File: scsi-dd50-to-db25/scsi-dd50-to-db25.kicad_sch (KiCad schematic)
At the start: 2 parts, among them J1 DD50_Plug_MountingHoles, J2 DB25_Socket_MountingHoles

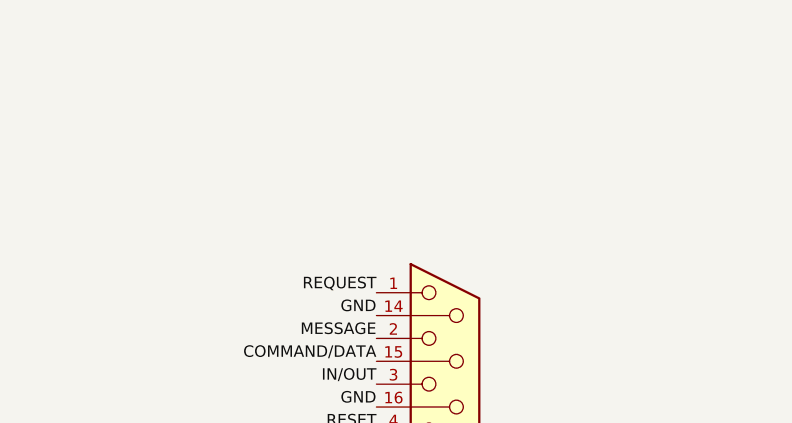
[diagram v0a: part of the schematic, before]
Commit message: Added a term power port for pulling 5v off to another adapter.
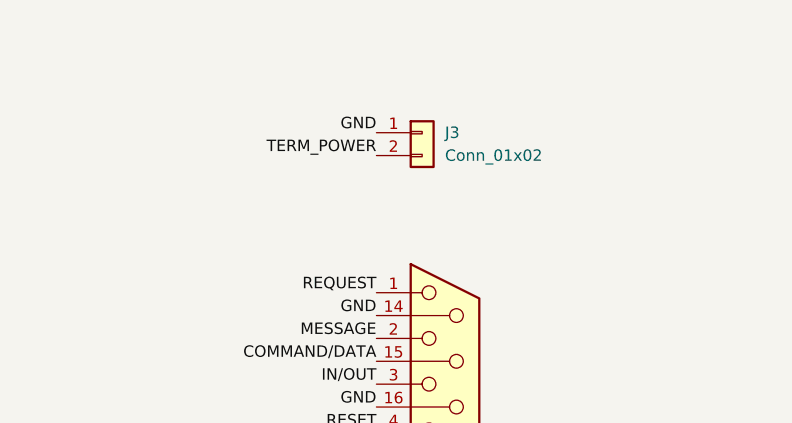
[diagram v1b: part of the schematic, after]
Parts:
- added J3: Conn_01x02, Connector_PinHeader_2.54mm:PinHeader_1x02_P2.54mm_Horizontal, symbol Connector_Generic:Conn_01x02
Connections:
- net GND: now also J3.1 (Pin_1)
- net TERM_POWER: now also J3.2 (Pin_2)
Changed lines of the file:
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@@
+		)
+	)
+	(label "GND"
+		(at 167.64 45.72 180)
+		(effects
+			(font
+				(size 1.27 1.27)
+			)
+			(justify right bottom)
 		)
 	)
 	(label "TERM_POWER"
 		(at 167.64 121.92 180)
+		(effects
+			(font
+				(size 1.27 1.27)
+			)
+			(justify right bottom)
+		)
+	)
+	(label "TERM_POWER"
+		(at 167.64 48.26 180)
 		(effects
 			(font
@@
 					(unit 1)
 				)
+			)
+		)
+	)
+	(symbol
+		(lib_id "Connector_Generic:Conn_01x02")
+		(at 172.72 45.72 0)
+		(unit 1)
+		(exclude_from_sim no)
+		(in_bom yes)
+		(on_board yes)
+		(dnp no)
+		(fields_autoplaced yes)
+		(property "Reference" "J3"
+			(at 175.26 45.7199 0)
+			(effects
+				(font
+					(size 1.27 1.27)
+				)
+				(justify left)
+			)
+		)
+		(property "Value" "Conn_01x02"
+			(at 175.26 48.2599 0)
+			(effects
+				(font
+					(size 1.27 1.27)
+				)
+				(justify left)
+			)
+		)
+		(property "Footprint" "Connector_PinHeader_2.54mm:PinHeader_1x02_P2.54mm_Horizontal"
+			(at 172.72 45.72 0)
+			(effects
+				(font
+					(size 1.27 1.27)
+				)
+				(hide yes)
+			)
+		)
+		(property "Datasheet" "~"
+			(at 172.72 45.72 0)
+			(effects
+				(font
+					(size 1.27 1.27)
+				)
+				(hide yes)
+			)
+		)
+		(property "Description" "Generic connector, single row, 01x02, script generated (kicad-library-utils/schlib/autogen/connector/)"
+			(at 172.72 45.72 0)
+			(effects
+				(font
+					(size 1.27 1.27)
+				)
+				(hide yes)
+			)
+		)
+		(pin "1"
+		)
+		(pin "2"
+		)
+		(instances
+			(project ""
+				(path "/4355ec7a-8fe5-41c6-bf79-94b58d7f3796"
+					(reference "J3")
+					(unit 1)
+				)

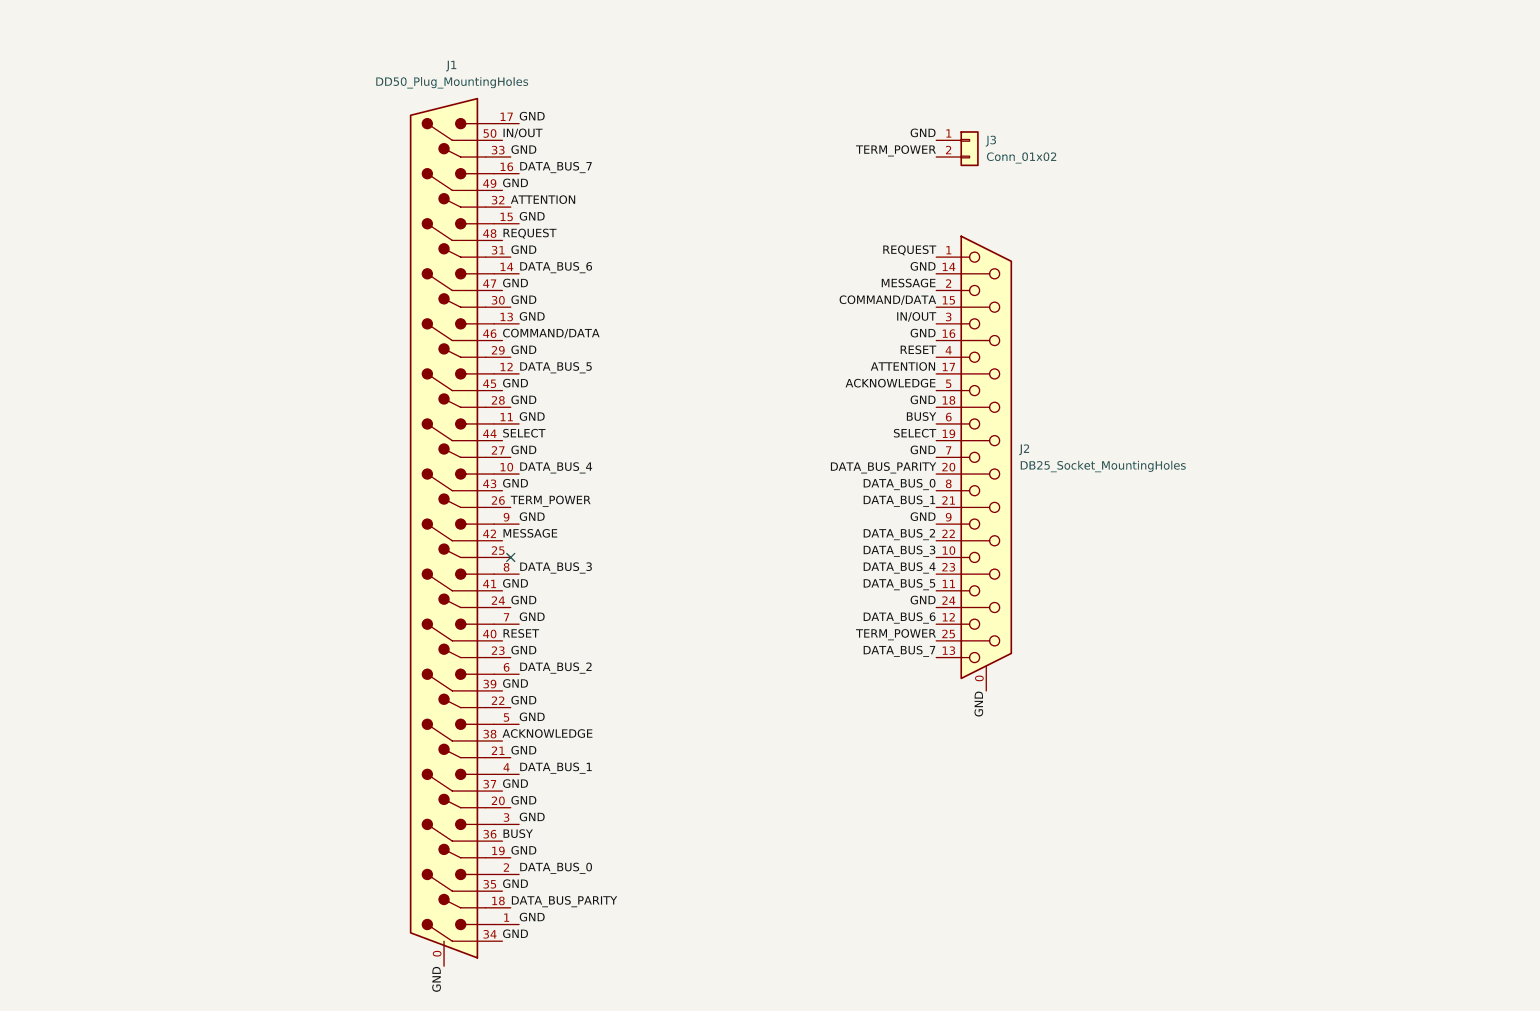
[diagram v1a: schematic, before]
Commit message: Fixing the pinout of the Sun Microsystems SCSI SE DD50 connector.
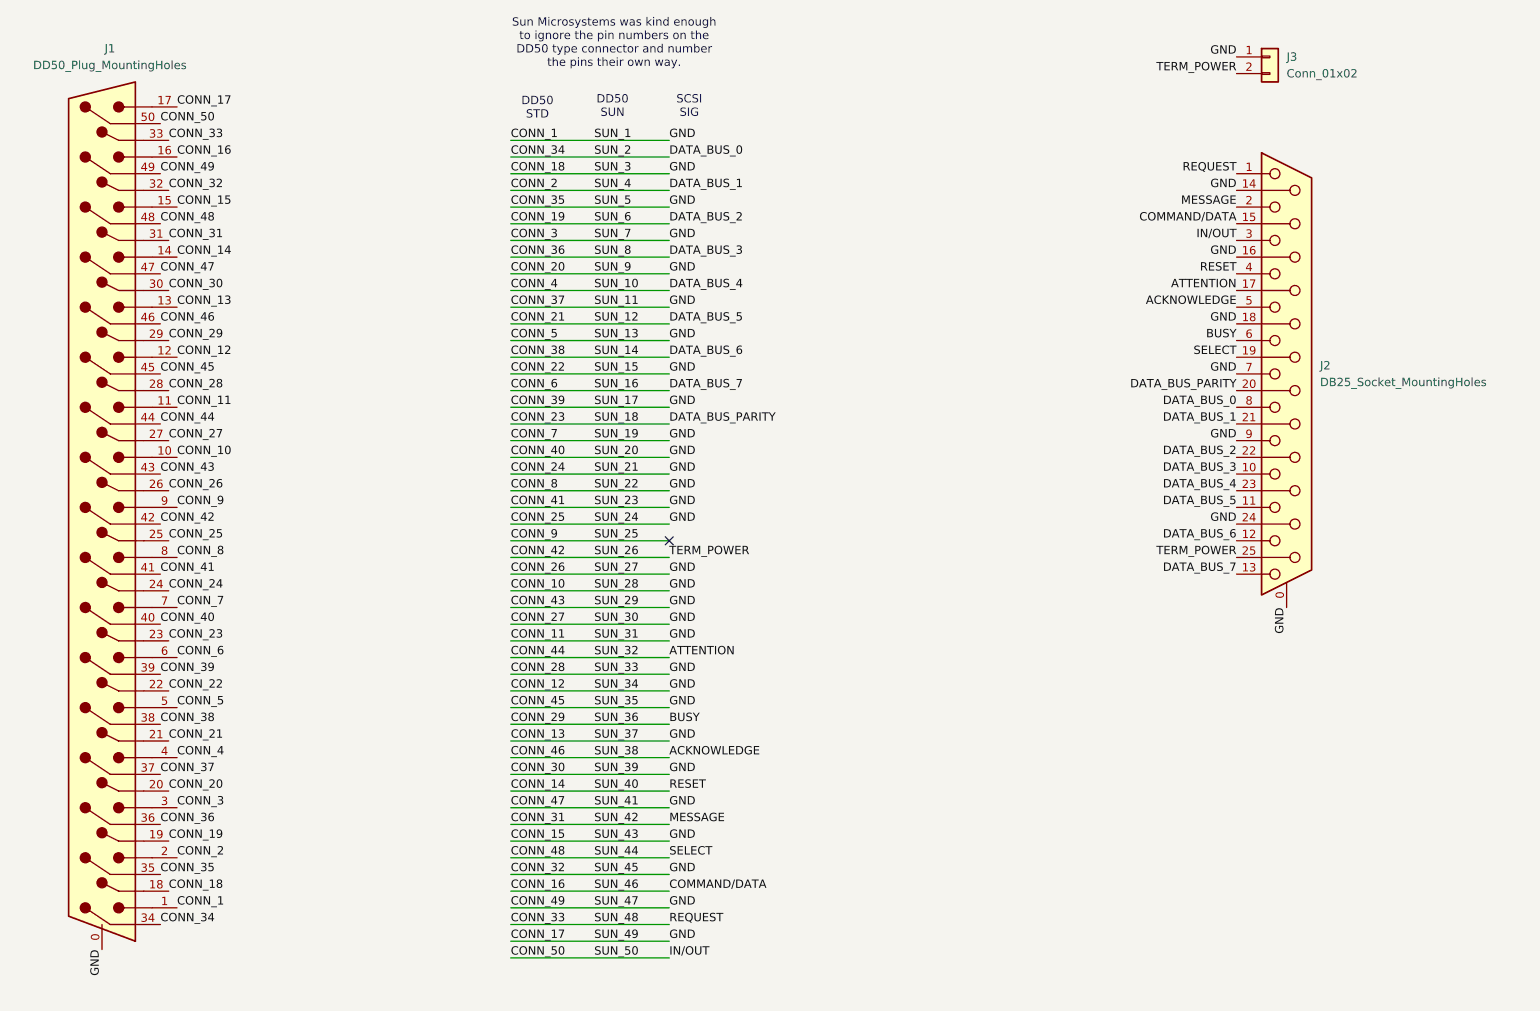
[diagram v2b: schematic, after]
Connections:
- net ACKNOWLEDGE: now also J1.46; no longer J1.38
- net ATTENTION: now also J1.44; no longer J1.32
- net BUSY: now also J1.29; no longer J1.36
- net COMMAND/DATA: now also J1.16; no longer J1.46
- net CONN_1: now reaches J1.25
- net CONN_1: now also J1.0, J1.1, J1.10, J1.11, J1.12, J1.13, J1.15, J1.17, J1.18, J1.20, J1.22, J1.24, J1.26, J1.27, J1.28, J1.3, J1.30, J1.32, J1.35, J1.37, J1.39, J1.40, J1.41, J1.43, J1.45, J1.47, J1.49, J1.5, J1.7, J1.8, J2.0 (PAD), J2.14 (P14), J2.16 (P16), J2.18 (P18), J2.24 (P24), J2.7, J2.9, J3.1 (Pin_1)
- net DATA_BUS_0 renamed CONN_2
- net CONN_2: now also J2.21 (P21); no longer J2.8
- net DATA_BUS_1 renamed CONN_4
- net CONN_4: now also J2.23 (P23); no longer J2.21 (P21)
- net DATA_BUS_2 renamed CONN_19
- net CONN_19: now also J1.19; no longer J1.6
- net DATA_BUS_3 renamed CONN_36
- net CONN_36: now also J1.36; no longer J1.8
- removed net DATA_BUS_4: J1.10, J2.23 (P23)
- net DATA_BUS_5 renamed CONN_21
- net CONN_21: now also J1.21; no longer J1.12
- net DATA_BUS_6 renamed CONN_14
- net CONN_14: now also J2.4; no longer J2.12
- net DATA_BUS_7 renamed CONN_6
- net CONN_6: now also J1.6; no longer J1.16
- net DATA_BUS_PARITY renamed CONN_23
- net CONN_23: now also J1.23; no longer J1.18
- removed net GND: J1.0, J1.1, J1.11, J1.13, J1.15, J1.17, J1.19, J1.20, J1.21, J1.22, J1.23, J1.24, J1.27, J1.28, J1.29, J1.3, J1.30, J1.31, J1.33, J1.34, J1.35, J1.37, J1.39, J1.41, J1.43, J1.45, J1.47, J1.49, J1.5, J1.7, J1.9, J2.0 (PAD), J2.14 (P14), J2.16 (P16), J2.18 (P18), J2.24 (P24), J2.7, J2.9, J3.1 (Pin_1)
- net IN/OUT renamed CONN_50
- net MESSAGE renamed CONN_31
- net CONN_31: now also J1.31; no longer J1.42
- net REQUEST renamed CONN_33
- net CONN_33: now also J1.33; no longer J1.48
- removed net RESET: J1.40, J2.4
- net SELECT renamed CONN_48
- net CONN_48: now also J1.48; no longer J1.44
- net TERM_POWER renamed CONN_42
- net CONN_42: now also J1.42; no longer J1.26
- new net CONN_34: J1.34, J2.8
- new net CONN_38: J1.38, J2.12
- new net CONN_9: J1.9
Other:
- note added: "DD50 STD"
- note added: "DD50 SUN"
- note added: "SCSI SIG"
- note added: "Sun Microsystems was kind enough to ignore the pin numbers on the DD50 type connector and number the pins their own way."
- moved on the sheet: J1, J2, J3
